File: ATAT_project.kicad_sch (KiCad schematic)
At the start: 5 parts

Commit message: Update
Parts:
- removed J?: Conn_01x10_Female, symbol Connector:Conn_01x10_Female
- removed SW?: SW_Push, symbol Switch:SW_Push
- added 2x5_stlinkv2: Conn_02x05_Odd_Even, symbol Connector_Generic:Conn_02x05_Odd_Even
- added C? (x6): C, symbol Device:C
- added PWM_Channels: Conn_01x11_Female, symbol Connector:Conn_01x11_Female
- added UART: Conn_01x03_Female, symbol Connector:Conn_01x03_Female
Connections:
- net GND: now also SW?.1, 2x5_stlinkv2.5 (Pin_5), 2x5_stlinkv2.6 (Pin_6), C?.2, C?.2, C?.2, C?.2, C?.2, C?.2, PWM_Channels.11 (Pin_11), UART.3 (Pin_3)
- net at U?.14 (PA0): now also PWM_Channels.1 (Pin_1)
- net at U?.15 (PA1): now also PWM_Channels.2 (Pin_2)
- net at U?.17 (PA3): now also PWM_Channels.3 (Pin_3)
- net +5V: now reaches U?.19 (VDD)
- net +5V: now also U?.32 (VDD), U?.48 (VDD), U?.64 (VDD), C?.1, C?.1, C?.1, C?.1, C?.1
- net at U?.22 (PA6): now also PWM_Channels.4 (Pin_4)
- net at U?.23 (PA7): now also PWM_Channels.5 (Pin_5)
- net at U?.26 (PB0): now also PWM_Channels.6 (Pin_6)
- net at U?.27 (PB1): now also PWM_Channels.7 (Pin_7)
- net at U?.29 (PB10): now also PWM_Channels.10 (Pin_10)
- net TX: now reaches U?.42 (PA9)
- net TX: now also UART.1 (Pin_1)
- net RX: now reaches U?.43 (PA10)
- net RX: now also UART.2 (Pin_2)
- net swdio: now reaches U?.46 (PA13)
- net swdio: now also 2x5_stlinkv2.4 (Pin_4)
- net swclk: now reaches U?.49 (PA14)
- net swclk: now also 2x5_stlinkv2.2 (Pin_2)
- net at U?.58 (PB6): now also PWM_Channels.8 (Pin_8)
- net at U?.59 (PB7): now also PWM_Channels.9 (Pin_9)
- net at U?.7 (NRST): now also SW?.2, C?.1
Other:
- moved on the sheet: SW?, U?

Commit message: Updated Schematic
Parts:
- removed U?: BLUENRG-MSCSA, WLCSP34_2P66X2P56_STM, symbol 2024-10-28_02-55-17:BLUENRG-MSCSA
- added C10: 0.1u, symbol Device:C
- added C11: 2.2u, symbol Device:C
- added C7: 10n, symbol Device:C
- added C8, C9: 1u, symbol Device:C
- added FB1: 120R, symbol Device:FerriteBead
- added SW2: SW_Push, symbol Switch:SW_Push
- added U2: SPBTLE-RF, RF_Module:ST_SPBTLE, symbol RF_Bluetooth:SPBTLE-RF
- C1: renamed from C?; value C -> 0.1u
- C2: renamed from C?; value C -> 10u
- C3, C4, C5, C6: renamed from C?; value C -> 100n
- gave numbers to parts that had none: 2
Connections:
- net +5V is gone; now on net +3V3: C2.1, C3.1, C4.1, C5.1, C6.1, U1.19 (VDD), U1.32 (VDD), U1.48 (VDD), U1.64 (VDD)
- net GND: now also U1.12 (VSSA), C10.2, C11.2, C7.2, C8.2, C9.2, SW2.1, U2.6 (GND)
- net +3V3: now reaches 2x5_stlinkv2.8 (Pin_8)
- net +3V3: now also U1.13 (VDDA), C7.1, C8.1, FB1.1, U2.5 (VIN)
- net at U1.10 (PC2): now also C10.1, SW2.2
- net at U1.16 (PA2): now also PWM_Channels.3 (Pin_3)
- net at U1.17 (PA3): now also PWM_Channels.4 (Pin_4); no longer PWM_Channels.3 (Pin_3)
- net at U1.21 (PA5): now also U2.7 (SPI_CLK)
- net at U1.22 (PA6): now also U2.8 (SPI_MISO); no longer PWM_Channels.4 (Pin_4)
- net at U1.23 (PA7): now also U2.9 (SPI_MOSI); no longer PWM_Channels.5 (Pin_5)
- net at U1.26 (PB0): now also PWM_Channels.5 (Pin_5); no longer PWM_Channels.6 (Pin_6)
- net at U1.27 (PB1): now also PWM_Channels.6 (Pin_6); no longer PWM_Channels.7 (Pin_7)
- net at U1.29 (PB10): now also U2.4 (SPI_IRQ); no longer PWM_Channels.10 (Pin_10)
- net at U1.30 (VCAP_1): now also C11.1
- net at U1.33 (PB12): now also U2.10 (SPI_~{CS})
- net at U1.37 (PC6): now also PWM_Channels.8 (Pin_8)
- net at U1.38 (PC7): now also PWM_Channels.7 (Pin_7)
- net at U1.58 (PB6): now also PWM_Channels.9 (Pin_9); no longer PWM_Channels.8 (Pin_8)
- net at U1.59 (PB7): now also PWM_Channels.10 (Pin_10); no longer PWM_Channels.9 (Pin_9)
- net at U1.9 (PC1): now also U2.11 (~{BT_RESET})
- new net: C9.1, FB1.2
- no-connect marks 0 -> 33
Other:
- moved on the sheet: 2x5_stlinkv2, C1, C2, C3, C4, C5, C6, PWM_Channels, SW1, U1, UART

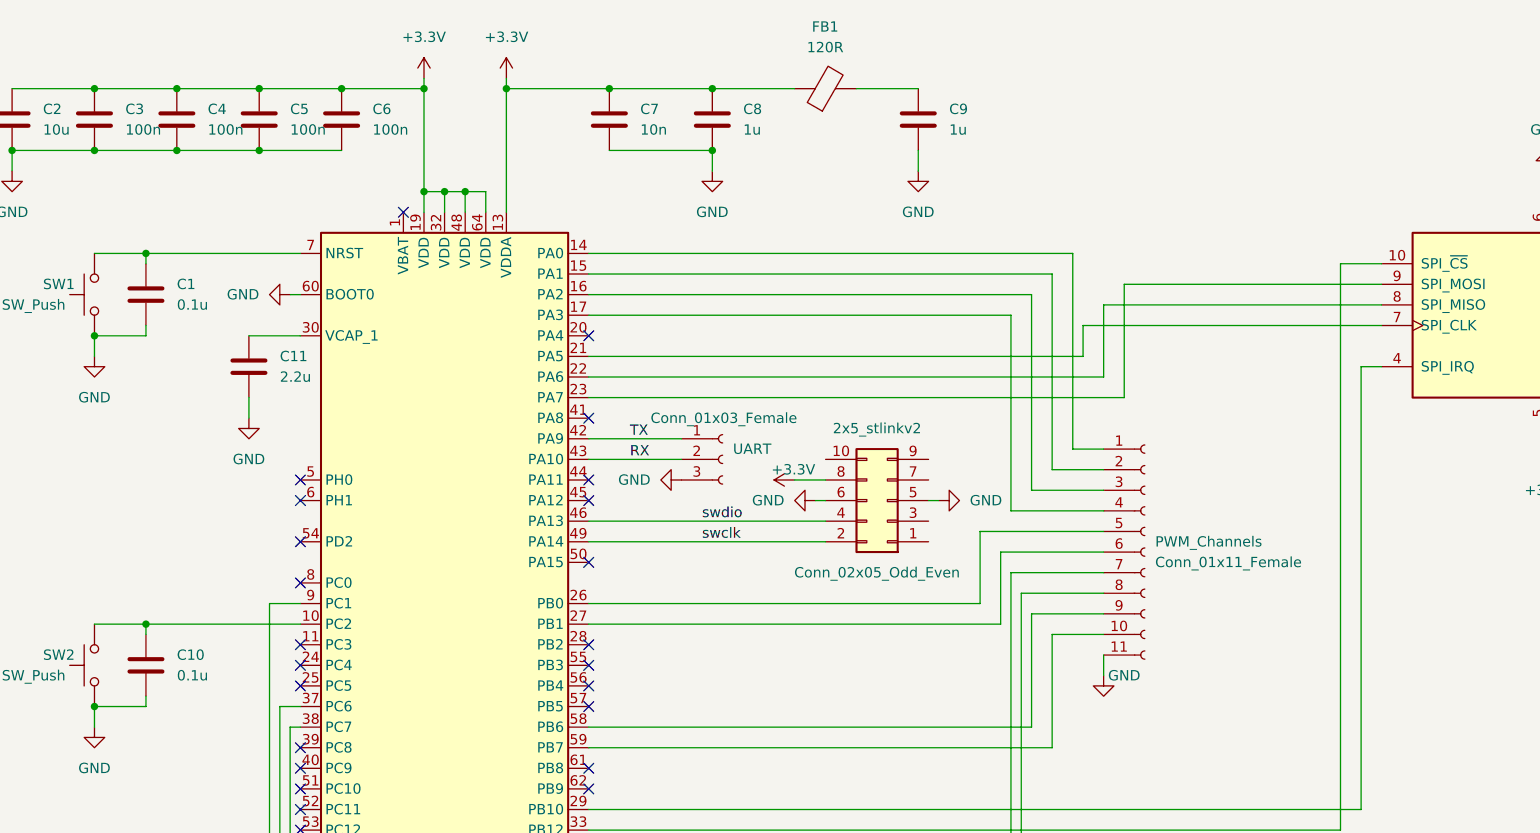
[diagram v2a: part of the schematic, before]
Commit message: Added footprints
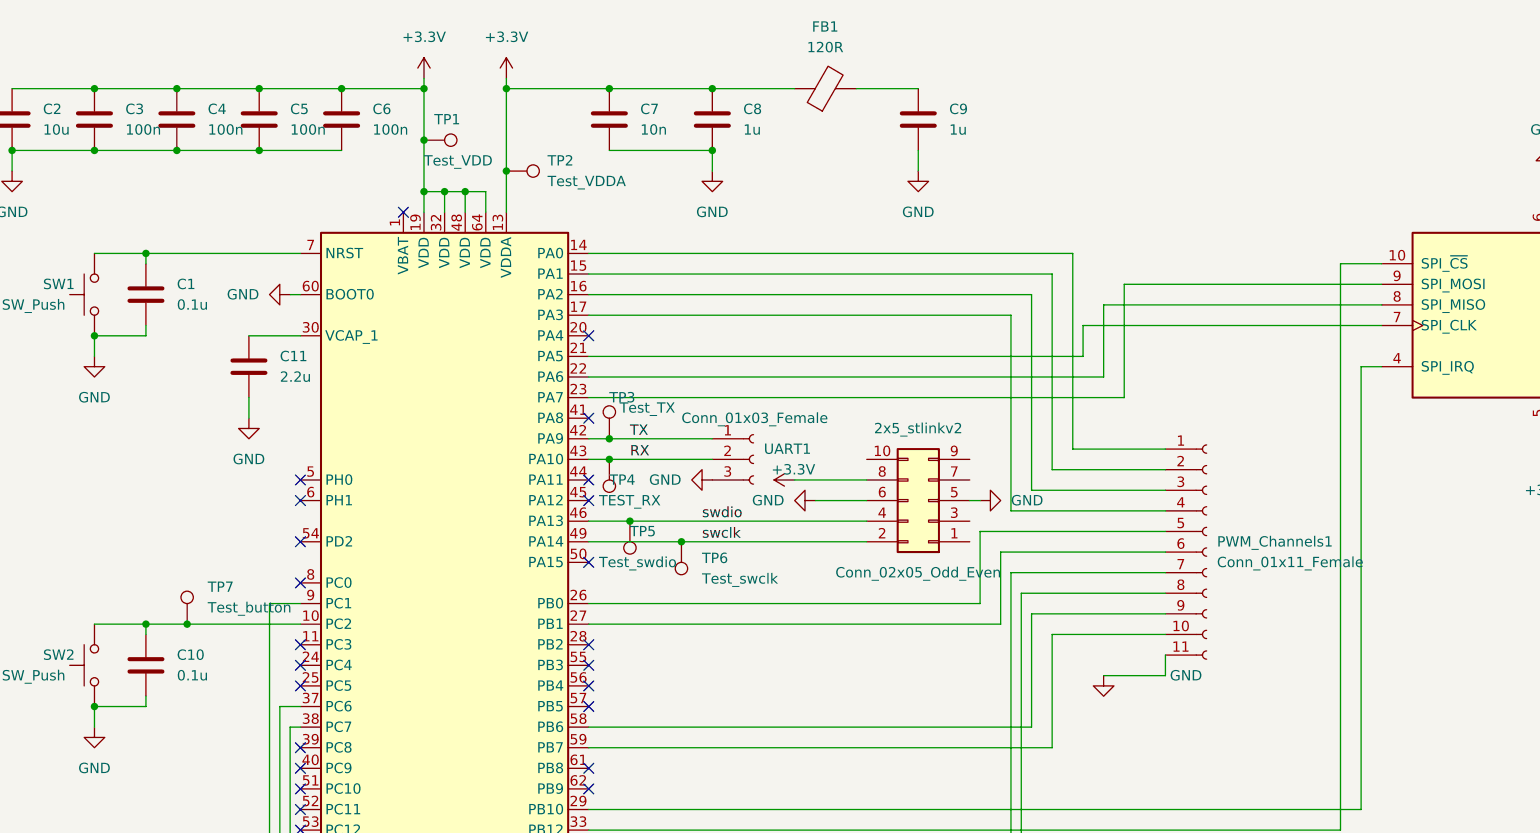
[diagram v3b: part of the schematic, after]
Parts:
- added TP1: Test_VDD, TestPoint:TestPoint_Keystone_5010-5014_Multipurpose, symbol Connector:TestPoint
- added TP2: Test_VDDA, TestPoint:TestPoint_Keystone_5010-5014_Multipurpose, symbol Connector:TestPoint
- added TP3: Test_TX, TestPoint:TestPoint_Keystone_5010-5014_Multipurpose, symbol Connector:TestPoint
- added TP4: TEST_RX, TestPoint:TestPoint_Keystone_5010-5014_Multipurpose, symbol Connector:TestPoint
- added TP5: Test_swdio, TestPoint:TestPoint_Keystone_5010-5014_Multipurpose, symbol Connector:TestPoint
- added TP6: Test_swclk, TestPoint:TestPoint_Keystone_5010-5014_Multipurpose, symbol Connector:TestPoint
- added TP7: Test_button, TestPoint:TestPoint_Keystone_5010-5014_Multipurpose, symbol Connector:TestPoint
- 2x5_stlinkv2: footprint (none) -> Connector_PinHeader_2.54mm:PinHeader_2x05_P2.54mm_Vertical
- C1, C10, C11, C2, C3, C4, C5, C6, C7, C8, C9: footprint (none) -> Capacitor_SMD:C_0805_2012Metric_Pad1.18x1.45mm_HandSolder
- FB1: footprint (none) -> Resistor_SMD:R_0805_2012Metric_Pad1.20x1.40mm_HandSolder
- PWM_Channels1: renamed from PWM_Channels; footprint (none) -> Connector_PinHeader_2.54mm:PinHeader_1x11_P2.54mm_Vertical
- SW1, SW2: footprint (none) -> Button_Switch_THT:SW_PUSH_6mm_H4.3mm
- UART1: renamed from UART; footprint (none) -> Connector_PinHeader_2.54mm:PinHeader_1x03_P2.54mm_Vertical
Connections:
- net +3V3: now also TP1.1, TP2.1
- net RX: now also TP4.1
- net TX: now also TP3.1
- net swclk: now also TP6.1
- net swdio: now also TP5.1
- net at C10.1, SW2.2, U1.10 (PC2): now also TP7.1
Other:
- moved on the sheet: 2x5_stlinkv2, PWM_Channels1, UART1

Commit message: scuffed but done
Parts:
- added C12: 100p, Capacitor_SMD:C_0805_2012Metric_Pad1.18x1.45mm_HandSolder, symbol Device:C
- added C13: 1u, Capacitor_SMD:C_0805_2012Metric_Pad1.18x1.45mm_HandSolder, symbol Device:C
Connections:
- net +3V3: now also C12.2, C13.2
- net GND: now also C12.1, C13.1

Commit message: Fixed all DRC, started Casey's feedback
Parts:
- removed TP2: Test_VDDA, TestPoint:TestPoint_Keystone_5010-5014_Multipurpose, symbol Connector:TestPoint
- removed TP5: Test_swdio, TestPoint:TestPoint_Keystone_5010-5014_Multipurpose, symbol Connector:TestPoint
- removed TP6: Test_swclk, TestPoint:TestPoint_Keystone_5010-5014_Multipurpose, symbol Connector:TestPoint
- removed UART1: Conn_01x03_Female, Connector_PinHeader_2.54mm:PinHeader_1x03_P2.54mm_Vertical, symbol Connector:Conn_01x03_Female
- added GND1: Test_GND, TestPoint:TestPoint_Keystone_5010-5014_Multipurpose, symbol Connector:TestPoint
- added R1, R2: 10k, Resistor_SMD:R_0805_2012Metric_Pad1.20x1.40mm_HandSolder, symbol Device:R
- added UART1: Conn_01x06_Socket, Connector_PinSocket_2.54mm:PinSocket_1x06_P2.54mm_Vertical, symbol Connector:Conn_01x06_Socket
- PWM_Channels1: footprint Connector_PinHeader_2.54mm:PinHeader_1x11_P2.54mm_Vertical -> Connector_PinSocket_2.54mm:PinSocket_1x11_P2.54mm_Vertical
- renumbered TP7 to Button1, SW1 to RESET1, TP4 to RX1, SW2 to Start/Stop1, TP3 to TX1, TP1 to VDD1, 2x5_stlinkv2 to stlinkv2
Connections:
- net +3V3: no longer C7.1, C8.1
- net GND: now also GND1.1, UART1.6 (Pin_6)
- net RX: now also UART1.2 (Pin_2)
- net TX: now also UART1.3 (Pin_3)
- net at C9.1, FB1.2: now also C7.1, C8.1
- net at Button1.1, C10.1, Start/Stop1.2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: now also R2.2
- net at C1.1, RESET1.2, U1.7 (NRST): now also R1.2
- new net +3.3V: R1.1, R2.1
- no-connect marks 33 -> 41
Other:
- moved on the sheet: C7, C8, FB1, PWM_Channels1, stlinkv2

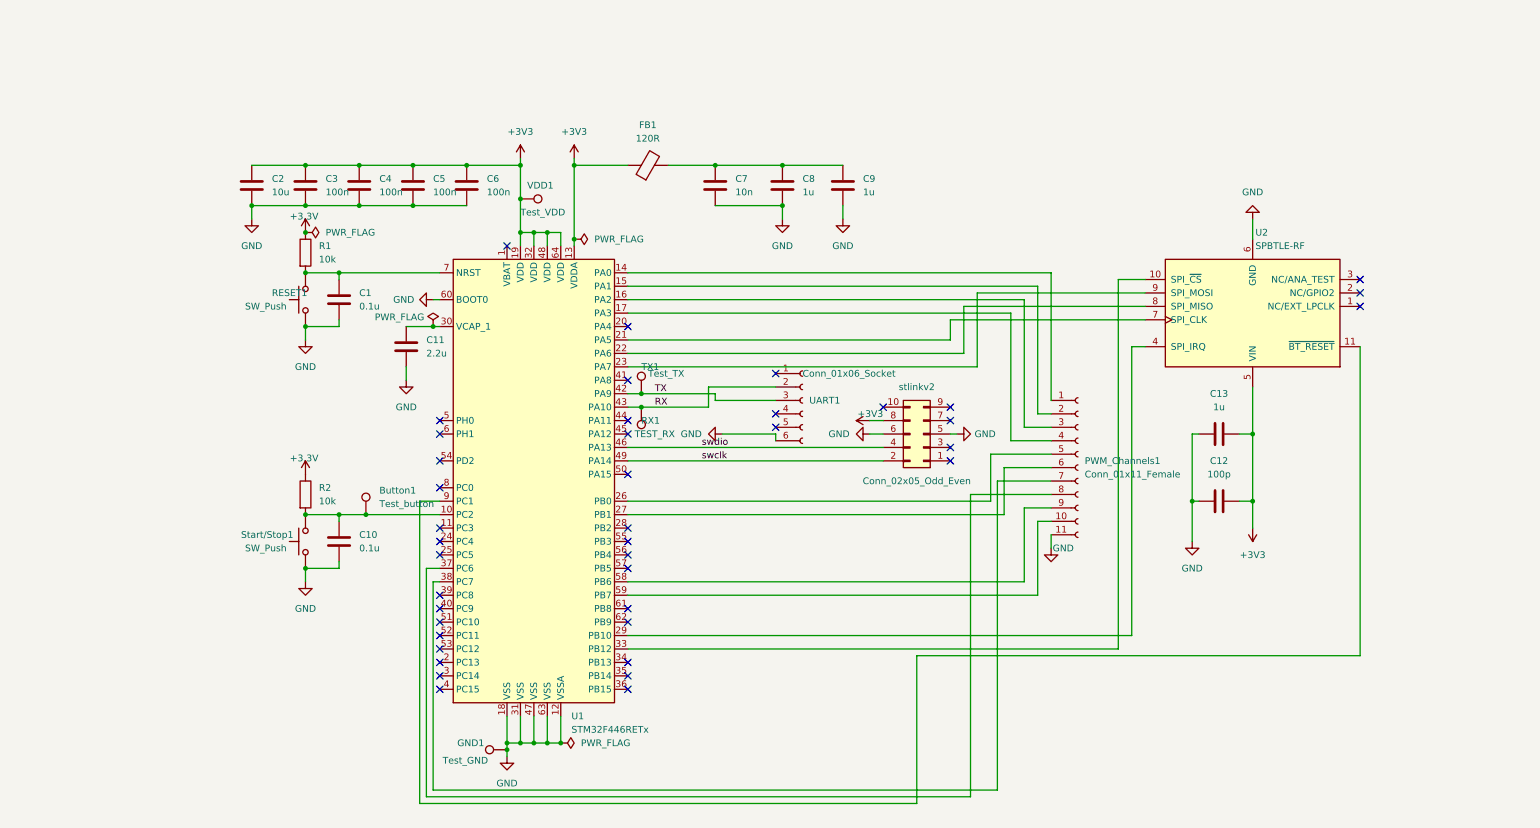
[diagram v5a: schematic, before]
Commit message: NEW SCHEMATIC! (Needs PCB Design)
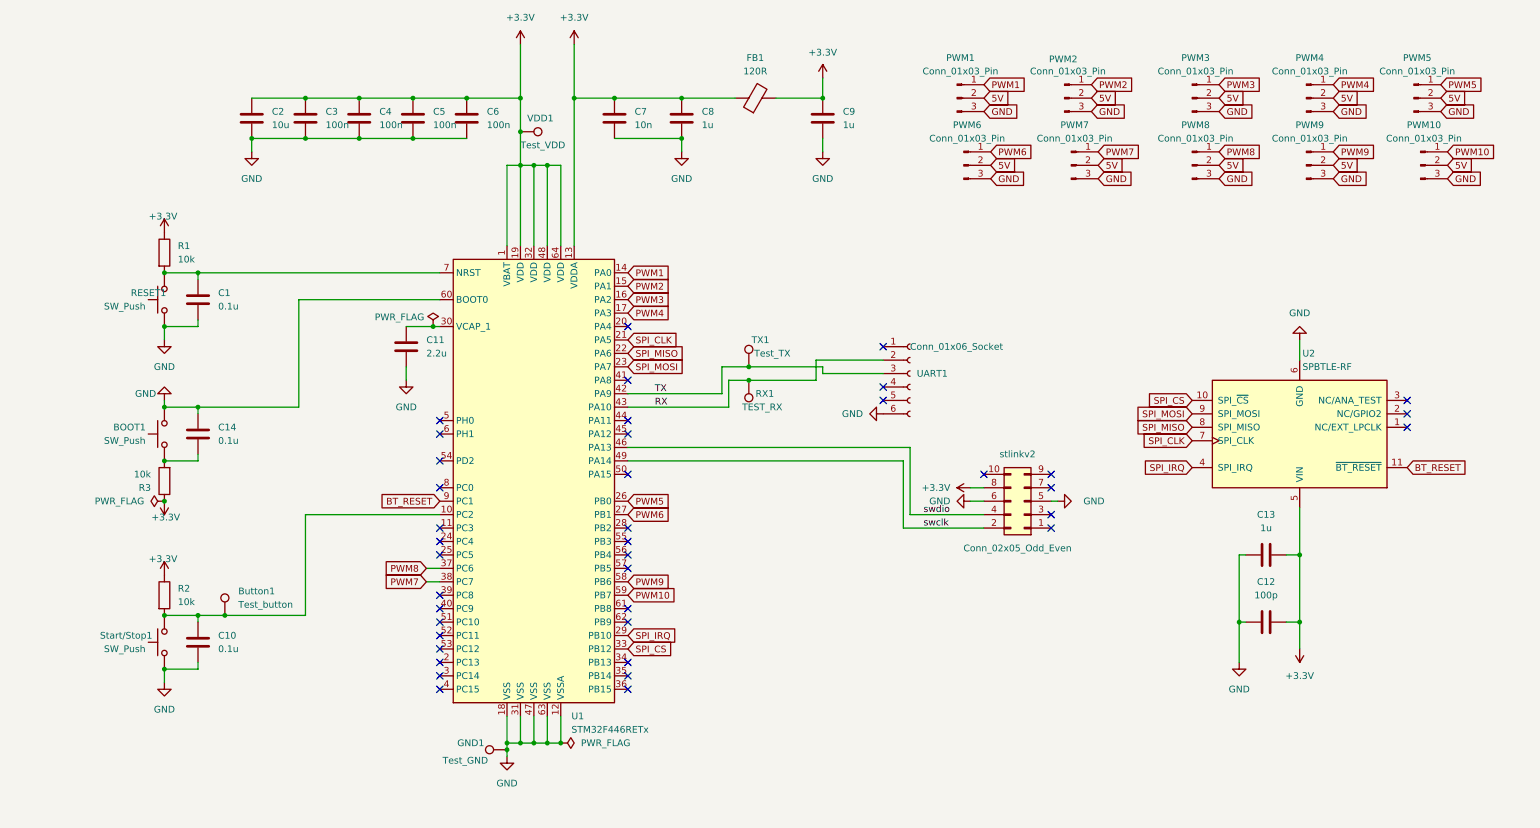
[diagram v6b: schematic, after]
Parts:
- removed PWM_Channels1: Conn_01x11_Female, Connector_PinSocket_2.54mm:PinSocket_1x11_P2.54mm_Vertical, symbol Connector:Conn_01x11_Female
- added BOOT1: SW_Push, Button_Switch_THT:SW_PUSH_6mm_H4.3mm, symbol Switch:SW_Push
- added C14: 0.1u, Capacitor_SMD:C_0805_2012Metric_Pad1.18x1.45mm_HandSolder, symbol Device:C
- added PWM1, PWM10, PWM2, PWM3, PWM4, PWM5, PWM6, PWM7, PWM8, PWM9: Conn_01x03_Pin, Connector_PinHeader_2.54mm:PinHeader_1x03_P2.54mm_Vertical, symbol Connector:Conn_01x03_Pin
- added R3: 10k, Resistor_SMD:R_0805_2012Metric_Pad1.20x1.40mm_HandSolder, symbol Device:R
- Button1, GND1, RX1, TX1, VDD1: footprint TestPoint:TestPoint_Keystone_5010-5014_Multipurpose -> TestPoint:TestPoint_Pad_D1.0mm
- UART1: footprint Connector_PinSocket_2.54mm:PinSocket_1x06_P2.54mm_Vertical -> Connector_PinSocket_2.54mm:PinSocket_1x06_P2.54mm_Horizontal
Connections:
- net +3V3 is gone; now on net +3.3V: C12.2, C13.2, C2.1, C3.1, C4.1, C5.1, C6.1, FB1.1, U1.13 (VDDA), U1.19 (VDD), U1.32 (VDD), U1.48 (VDD), U1.64 (VDD), U2.5 (VIN), VDD1.1, stlinkv2.8 (Pin_8)
- net +3.3V: now also C7.1, C8.1, C9.1, FB1.2, U1.1 (VBAT), R3.1
- net GND: now also BOOT1.2, C14.1, PWM1.3 (Pin_3), PWM10.3 (Pin_3), PWM2.3 (Pin_3), PWM3.3 (Pin_3), PWM4.3 (Pin_3), PWM5.3 (Pin_3), PWM6.3 (Pin_3), PWM7.3 (Pin_3), PWM8.3 (Pin_3), PWM9.3 (Pin_3)
- net PWM1: now reaches U1.14 (PA0)
- net PWM1: now also PWM1.1 (Pin_1)
- net PWM2: now reaches U1.15 (PA1)
- net PWM2: now also PWM2.1 (Pin_1)
- net PWM3: now reaches U1.16 (PA2)
- net PWM3: now also PWM3.1 (Pin_1)
- net PWM4: now reaches U1.17 (PA3)
- net PWM4: now also PWM4.1 (Pin_1)
- net SPI_CLK: now reaches U1.21 (PA5), U2.7 (SPI_CLK)
- net SPI_MISO: now reaches U1.22 (PA6), U2.8 (SPI_MISO)
- net SPI_MOSI: now reaches U1.23 (PA7), U2.9 (SPI_MOSI)
- net PWM5: now reaches U1.26 (PB0)
- net PWM5: now also PWM5.1 (Pin_1)
- net PWM6: now reaches U1.27 (PB1)
- net PWM6: now also PWM6.1 (Pin_1)
- net SPI_IRQ: now reaches U1.29 (PB10), U2.4 (SPI_IRQ)
- net SPI_CS: now reaches U1.33 (PB12), U2.10 (SPI_~{CS})
- net PWM8: now reaches U1.37 (PC6)
- net PWM8: now also PWM8.1 (Pin_1)
- net PWM7: now reaches U1.38 (PC7)
- net PWM7: now also PWM7.1 (Pin_1)
- net PWM9: now reaches U1.58 (PB6)
- net PWM9: now also PWM9.1 (Pin_1)
- net PWM10: now reaches U1.59 (PB7)
- net PWM10: now also PWM10.1 (Pin_1)
- net BT_RESET: now reaches U1.9 (PC1), U2.11 (~{BT_RESET})
- new net: BOOT1.1, C14.2, R3.2
- new net 5V: PWM1.2 (Pin_2), PWM10.2 (Pin_2), PWM2.2 (Pin_2), PWM3.2 (Pin_2), PWM4.2 (Pin_2), PWM5.2 (Pin_2), PWM6.2 (Pin_2), PWM7.2 (Pin_2), PWM8.2 (Pin_2), PWM9.2 (Pin_2)
- no-connect marks 41 -> 40
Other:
- moved on the sheet: Button1, C1, C10, C12, C13, C2, C3, C4, C5, C6, C7, C8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

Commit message: NEW PCB!!!
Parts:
- added 5V1: Test_5V, TestPoint:TestPoint_Pad_D1.0mm, symbol Connector:TestPoint
- added C15: 100n, Capacitor_SMD:C_0805_2012Metric_Pad1.18x1.45mm_HandSolder, symbol Device:C
- added J1: Conn_01x03_Socket, Connector_PinSocket_2.54mm:PinSocket_1x03_P2.54mm_Vertical, symbol Connector:Conn_01x03_Socket
- added TP1, TP10, TP2, TP3, TP4, TP5, TP6, TP7, TP8, TP9: Test_PWM, TestPoint:TestPoint_Pad_D1.0mm, symbol Connector:TestPoint
- UART1: footprint Connector_PinSocket_2.54mm:PinSocket_1x06_P2.54mm_Horizontal -> Connector_PinSocket_2.54mm:PinSocket_1x06_P2.54mm_Vertical
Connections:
- net +3.3V: now also C15.1, J1.1 (Pin_1)
- net GND: now also UART1.1 (Pin_1), C15.2, J1.2 (Pin_2); no longer UART1.6 (Pin_6)
- net PWM1: now also TP1.1
- net PWM10: now also TP10.1
- net PWM2: now also TP2.1
- net PWM3: now also TP3.1
- net PWM4: now also TP4.1
- net PWM5: now also TP5.1
- net PWM6: now also TP6.1
- net PWM7: now also TP7.1
- net PWM8: now also TP8.1
- net PWM9: now also TP9.1
- net MCU_RX: now reaches UART1.4 (Pin_4)
- net MCU_RX: now also RX1.1, U1.43 (PA10)
- net MCU_TX: now reaches UART1.5 (Pin_5)
- net MCU_TX: now also TX1.1, U1.42 (PA9)
- net 5V renamed +5V
- net +5V: now also 5V1.1, J1.3 (Pin_3)
- removed net RX: RX1.1, U1.43 (PA10), UART1.2 (Pin_2)
- removed net TX: TX1.1, U1.42 (PA9), UART1.3 (Pin_3)
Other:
- moved on the sheet: C2, C3, C4, C5, C6, PWM1, RX1, TX1
